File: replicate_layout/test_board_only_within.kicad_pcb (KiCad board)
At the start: 2 copper layers, 39 parts, among them J1001 Pusa_4mm, J1002 Pusa_4mm, Q1001 CSD19531KCS, Q1002 CSD19531KCS, Q1003 CSD19531KCS, Q1004 CSD19531KCS, Q2001 CSD19531KCS, Q2002 CSD19531KCS, Q3001 CSD19531KCS, Q3002 CSD19531KCS, Q4001 CSD19531KCS, Q4002 CSD19531KCS, Q5001 CSD19531KCS, Q5002 CSD19531KCS, U1001 LAUNCHXL-F28377S, U2001 IR2181, U3001 IR2181, U4001 IR2181, U5001 IR2181

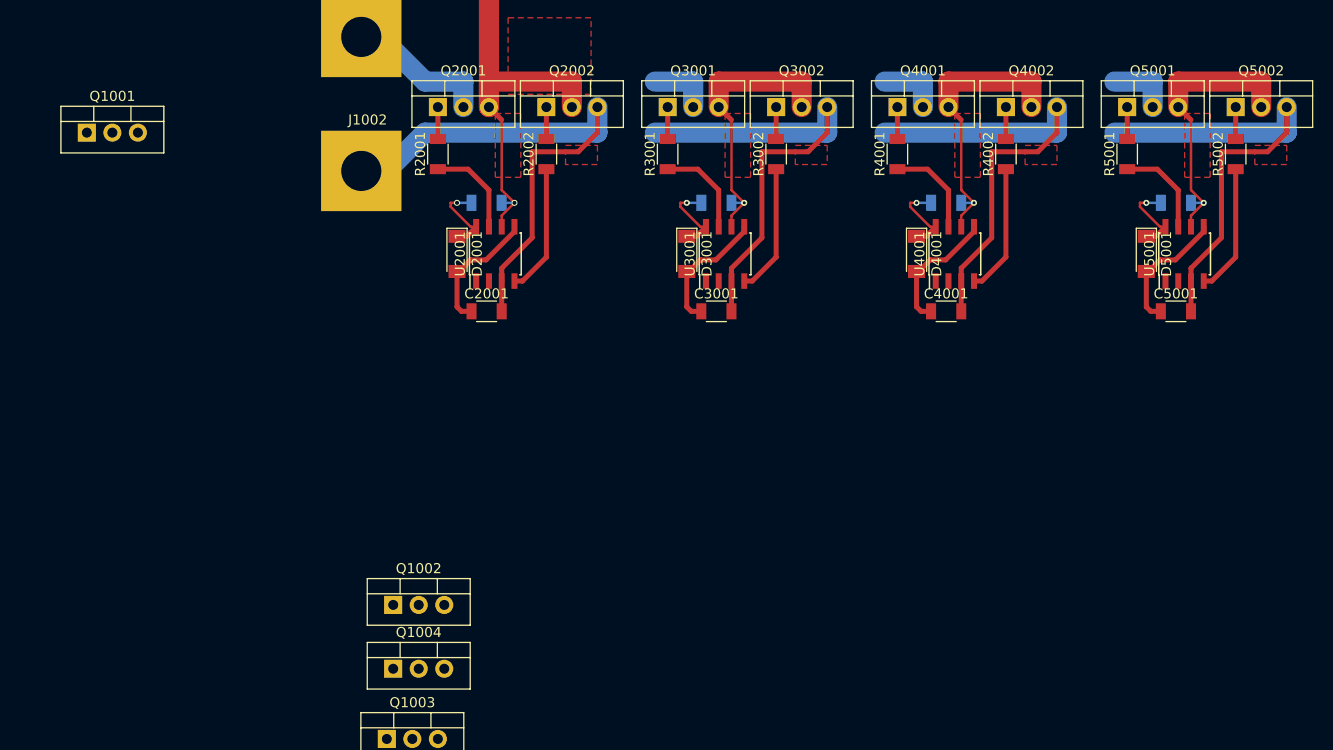
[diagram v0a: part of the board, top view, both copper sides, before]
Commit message: Added option to remove tracks/zones Updated documentation
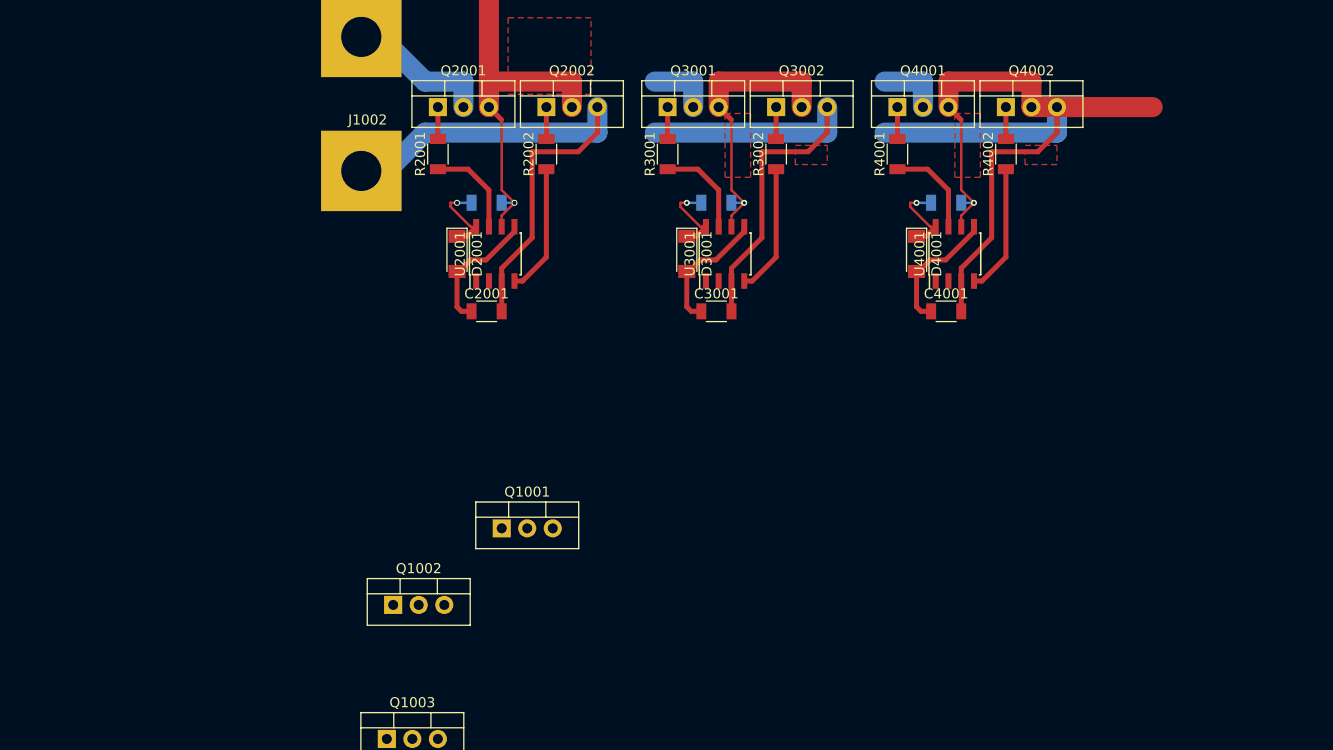
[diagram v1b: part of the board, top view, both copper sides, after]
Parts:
- removed C5001, C5002: 100n, Passives:RC1206M
- removed D5001: LL4148, Discretes:D_MiniMELF
- removed Q1004, Q5001, Q5002: CSD19531KCS, Discretes:TO-220
- removed R5001, R5002: 20, Passives:RC1206M
- removed U5001: IR2181, ICs:SO8
- moved Q1001 57.0 mm to (182.2, 128.3)
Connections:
- Q1001 pad 2: Net-(Q1001-Pad2) -> (no net)
- Q1001 pad 3: Net-(Q1001-Pad3) -> (no net)
- Q1002 pad 2: Net-(Q1002-Pad2) -> (no net)
- Q1002 pad 3: Net-(Q1002-Pad3) -> (no net)
- Q1003 pad 2: Net-(Q1003-Pad2) -> (no net)
- Q1003 pad 3: Net-(Q1003-Pad3) -> (no net)
- U1001 pad 1: Net-(U1001-Pad1) -> (no net)
- U1001 pad 10: Net-(U1001-Pad10) -> (no net)
- U1001 pad 11: Net-(U1001-Pad11) -> (no net)
- U1001 pad 13: Net-(U1001-Pad13) -> /Veja_1/HIN
- U1001 pad 14: /Veja_1/HIN -> (no net)
- U1001 pad 15: Net-(U1001-Pad15) -> (no net)
- U1001 pad 16: Net-(U1001-Pad16) -> (no net)
- U1001 pad 17: Net-(U1001-Pad17) -> (no net)
- U1001 pad 18: Net-(U1001-Pad18) -> (no net)
- U1001 pad 19: Net-(U1001-Pad19) -> (no net)
- U1001 pad 2: Net-(U1001-Pad2) -> (no net)
- U1001 pad 20: Net-(U1001-Pad20) -> (no net)
- U1001 pad 21: Net-(U1001-Pad21) -> (no net)
- U1001 pad 22: Net-(U1001-Pad22) -> (no net)
- U1001 pad 23: Net-(U1001-Pad23) -> (no net)
- U1001 pad 24: Net-(U1001-Pad24) -> (no net)
- U1001 pad 25: Net-(U1001-Pad25) -> (no net)
- U1001 pad 26: Net-(U1001-Pad26) -> (no net)
- U1001 pad 27: Net-(U1001-Pad27) -> (no net)
- U1001 pad 28: Net-(U1001-Pad28) -> (no net)
- U1001 pad 29: Net-(U1001-Pad29) -> (no net)
- U1001 pad 3: Net-(U1001-Pad3) -> (no net)
- U1001 pad 30: Net-(U1001-Pad30) -> (no net)
- U1001 pad 31: Net-(U1001-Pad31) -> (no net)
- U1001 pad 32: Net-(U1001-Pad32) -> (no net)
- U1001 pad 33: Net-(U1001-Pad33) -> (no net)
- U1001 pad 35: Net-(U1001-Pad35) -> /Veja_2/HIN
- U1001 pad 36: /Veja_2/HIN -> (no net)
- U1001 pad 37: Net-(U1001-Pad37) -> (no net)
- U1001 pad 38: Net-(U1001-Pad38) -> (no net)
- U1001 pad 39: Net-(U1001-Pad39) -> (no net)
- U1001 pad 4: Net-(U1001-Pad4) -> (no net)
- U1001 pad 40: Net-(U1001-Pad40) -> (no net)
- U1001 pad 41: Net-(U1001-Pad41) -> (no net)
- U1001 pad 42: Net-(U1001-Pad42) -> (no net)
- U1001 pad 43: Net-(U1001-Pad43) -> (no net)
- U1001 pad 44: Net-(U1001-Pad44) -> (no net)
- U1001 pad 45: Net-(U1001-Pad45) -> (no net)
- U1001 pad 46: Net-(U1001-Pad46) -> (no net)
- U1001 pad 47: Net-(U1001-Pad47) -> (no net)
- U1001 pad 48: Net-(U1001-Pad48) -> (no net)
- U1001 pad 49: Net-(U1001-Pad49) -> (no net)
- U1001 pad 5: Net-(U1001-Pad5) -> (no net)
- U1001 pad 50: Net-(U1001-Pad50) -> (no net)
- U1001 pad 51: Net-(U1001-Pad51) -> (no net)
- U1001 pad 52: /Veja_4/HIN -> (no net)
- U1001 pad 53: Net-(U1001-Pad53) -> (no net)
- U1001 pad 54: Net-(U1001-Pad54) -> (no net)
- U1001 pad 55: Net-(U1001-Pad55) -> (no net)
- U1001 pad 57: /Veja_3/LIN -> (no net)
- U1001 pad 58: Net-(U1001-Pad58) -> (no net)
- U1001 pad 6: Net-(U1001-Pad6) -> (no net)
- U1001 pad 60: Net-(U1001-Pad60) -> (no net)
- U1001 pad 61: Net-(U1001-Pad61) -> (no net)
- U1001 pad 62: Net-(U1001-Pad62) -> (no net)
- U1001 pad 63: Net-(U1001-Pad63) -> (no net)
- U1001 pad 64: Net-(U1001-Pad64) -> (no net)
- U1001 pad 65: Net-(U1001-Pad65) -> (no net)
- U1001 pad 66: Net-(U1001-Pad66) -> (no net)
- U1001 pad 67: Net-(U1001-Pad67) -> (no net)
- U1001 pad 68: Net-(U1001-Pad68) -> (no net)
- U1001 pad 69: Net-(U1001-Pad69) -> (no net)
- U1001 pad 7: Net-(U1001-Pad7) -> (no net)
- U1001 pad 70: Net-(U1001-Pad70) -> (no net)
- U1001 pad 71: Net-(U1001-Pad71) -> (no net)
- U1001 pad 72: Net-(U1001-Pad72) -> (no net)
- U1001 pad 73: Net-(U1001-Pad73) -> (no net)
- U1001 pad 74: Net-(U1001-Pad74) -> (no net)
- U1001 pad 75: Net-(U1001-Pad75) -> (no net)
- U1001 pad 76: Net-(U1001-Pad76) -> (no net)
- U1001 pad 77: Net-(U1001-Pad77) -> (no net)
- U1001 pad 78: Net-(U1001-Pad78) -> (no net)
- U1001 pad 79: Net-(U1001-Pad79) -> (no net)
- U1001 pad 8: Net-(U1001-Pad8) -> (no net)
- U1001 pad 80: /Veja_4/LIN -> (no net)
- U1001 pad 9: Net-(U1001-Pad9) -> (no net)
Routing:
- net GND: track 194.5 -> 147.8 mm
- net /Veja_4/OUT: track 28.1 -> 0.00 mm, vias 1 -> 0
- net +12V: track 51.9 -> 39.0 mm
- net /Veja_4/test/zaj: track 12.9 -> 0.00 mm
- net /Veja_3/OUT: track 28.1 -> 40.2 mm
- net Net-(R5001-Pad1): track 9.59 -> 0.00 mm
- net Net-(C5002-Pad1): track 8.13 -> 0.00 mm, vias 1 -> 0
- net +VDC: track 33.6 -> 27.2 mm
- net /Veja_4/QL_G: track 3.17 -> 0.00 mm
- net /Veja_4/QH_G: track 3.17 -> 0.00 mm
- removed copper zone on F.Cu, net /Veja_4/OUT
